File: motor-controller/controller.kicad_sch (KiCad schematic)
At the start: 20 parts

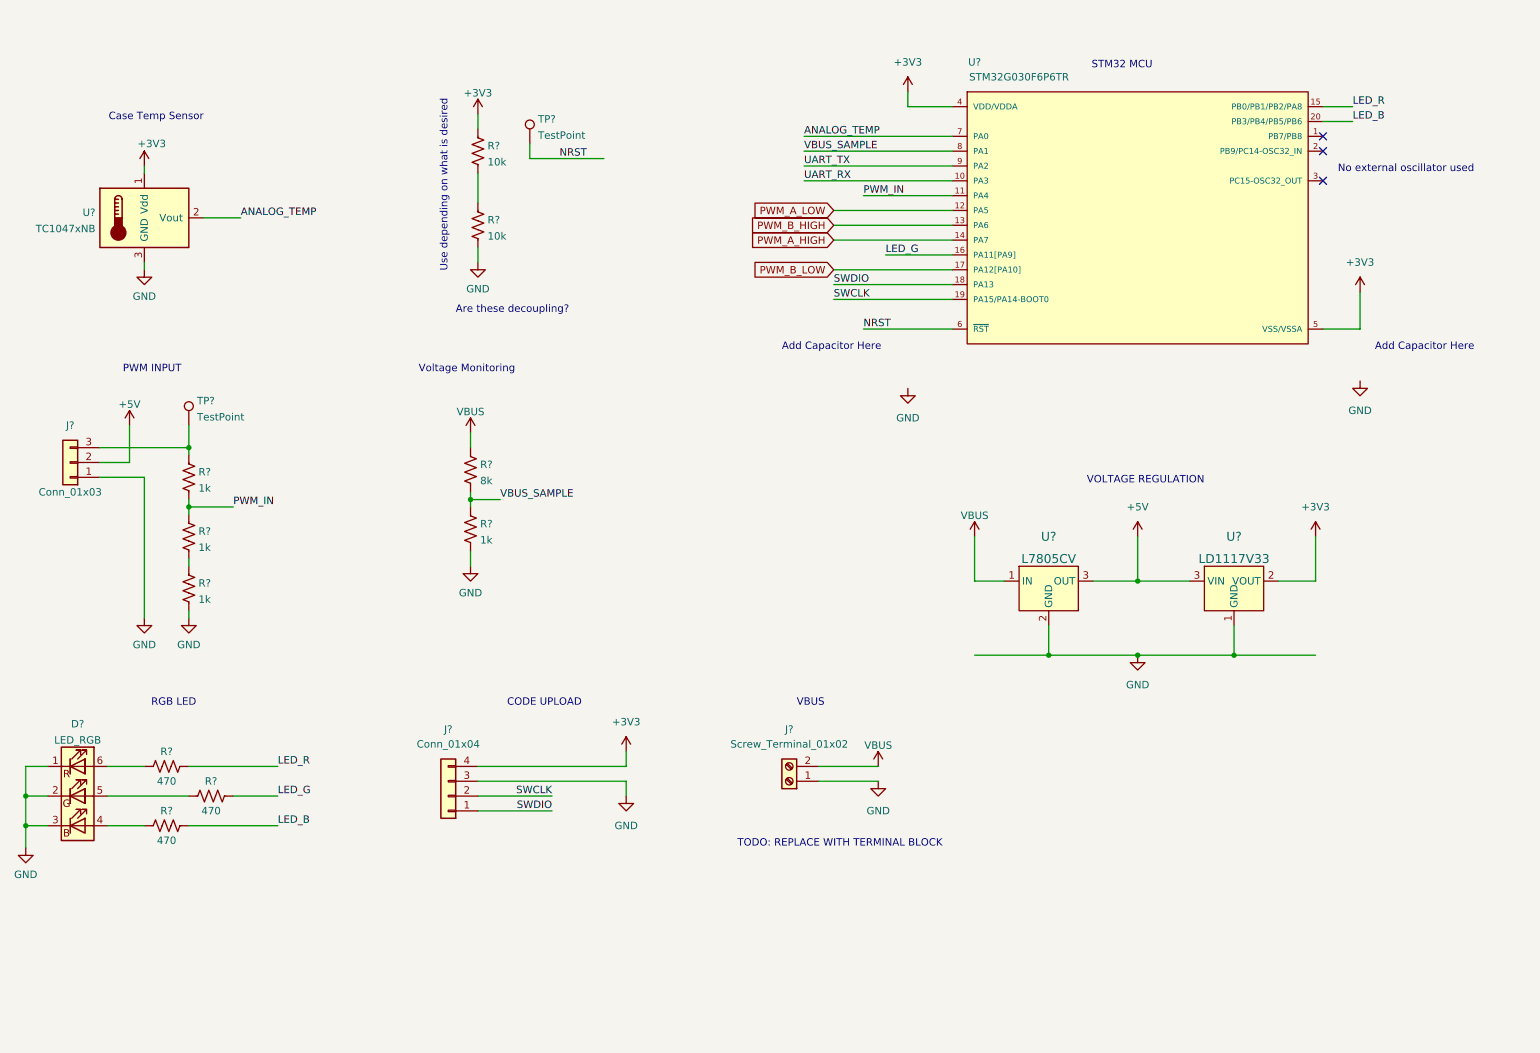
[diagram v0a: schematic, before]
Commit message: Minor schematic changes
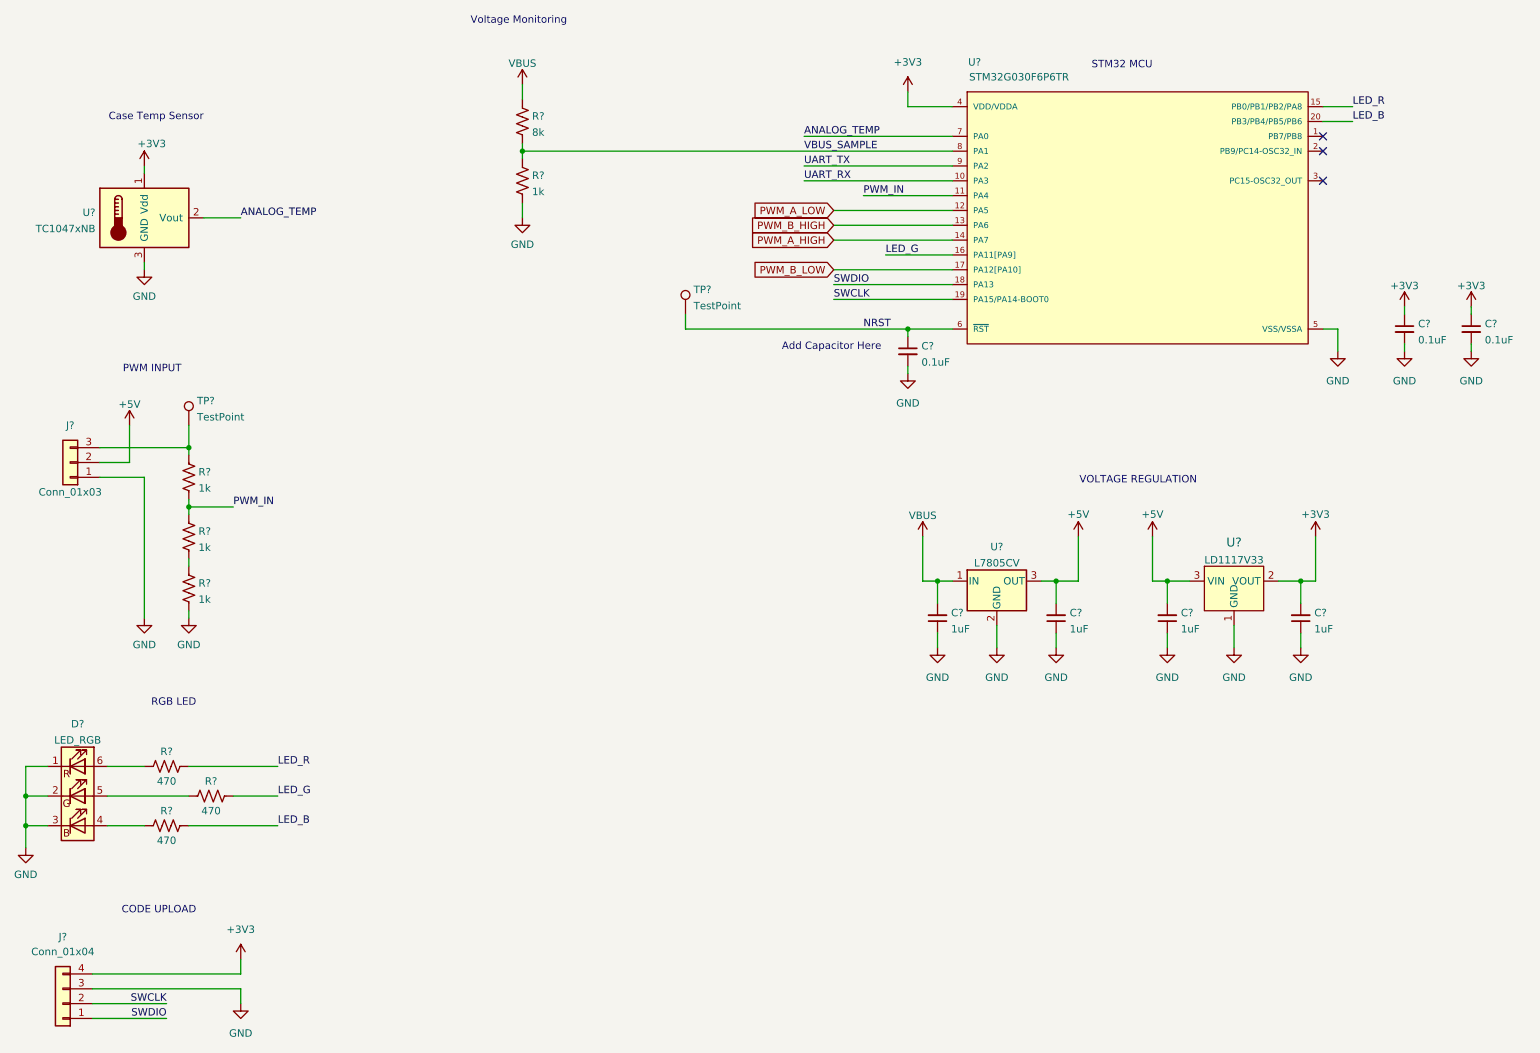
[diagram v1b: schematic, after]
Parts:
- removed J?: Screw_Terminal_01x02, TerminalBlock:TerminalBlock_bornier-2_P5.08mm, symbol Connector:Screw_Terminal_01x02
- removed R? (x2): 10k, symbol Device:R_US
- removed U?: L7805CV, digikey-footprints:TO-220-3, symbol dk_PMIC-Voltage-Regulators-Linear:L7805CV
- added C? (x3): 0.1uF, symbol Device:C_Small
- added C? (x4): 1uF, symbol Device:C_Small
- added U?: L7805CV, symbol Regulator_Linear:L7805
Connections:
- net +3V3: now also C?.1, C?.1, C?.2; no longer U?.5 (VSS/VSSA)
- net +5V: now also C?.2, C?.2, U?.3 (OUT)
- net GND: now also U?.5 (VSS/VSSA), C?.1, C?.1, C?.1, C?.1, C?.2, C?.2, C?.2, U?.2 (GND)
- net NRST: now also C?.1
- net VBUS: now also C?.2, U?.1 (IN)
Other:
- note removed: "Are these decoupling?"
- note removed: "No external oscillator used"
- note removed: "TODO: REPLACE WITH TERMINAL BLOCK"
- note removed: "Use depending on what is desired"
- note removed: "VBUS"
- moved on the sheet: J?, R?, TP?
